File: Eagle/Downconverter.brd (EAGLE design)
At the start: 40 x 40 mm, 26 parts, among them J2 3.5HEADPHONEJACK, J5 U.FL_CONN, J6 U.FL_CONN, U1 5V_REG, U2 MIXER, U3 DUAL_OP_AMP_LMV822, U4 DIGITAL_POTDIGITAL_POT

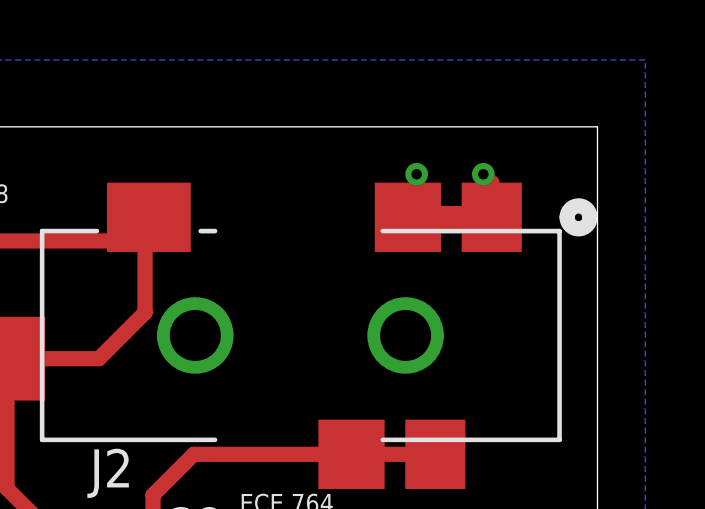
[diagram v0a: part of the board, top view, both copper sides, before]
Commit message: Updated Eagle to 9.4
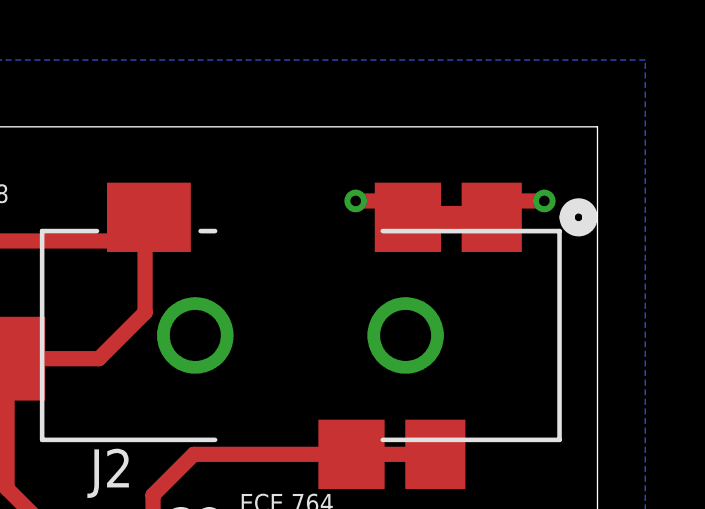
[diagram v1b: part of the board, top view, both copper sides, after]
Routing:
- net GND: track 44.1 -> 45.3 mm
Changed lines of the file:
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@@
 <wire x1="9.74" y1="36.195" x2="11.43" y2="36.195" width="0.762" layer="1"/>
 <via x="11.43" y="36.195" extent="1-16" drill="0.8"/>
-<wire x1="33.6804" y1="36.983" x2="33.9725" y2="37.2751" width="0.508" layer="1"/>
-<wire x1="33.9725" y1="37.2751" x2="33.9725" y2="38.4175" width="0.508" layer="1"/>
-<via x="33.9725" y="38.4175" extent="1-16" drill="0.35"/>
+<wire x1="33.6804" y1="36.983" x2="33.1349" y2="37.5285" width="0.508" layer="1"/>
+<wire x1="33.1349" y1="37.5285" x2="31.9405" y2="37.5285" width="0.508" layer="1"/>
+<via x="31.9405" y="37.5285" extent="1-16" drill="0.35"/>
 <wire x1="36.4744" y1="36.983" x2="36.322" y2="37.1354" width="0.508" layer="1"/>
-<wire x1="36.4744" y1="36.983" x2="36.4744" y2="38.1381" width="0.508" layer="1"/>
-<wire x1="36.4744" y1="38.1381" x2="36.195" y2="38.4175" width="0.508" layer="1"/>
-<via x="36.195" y="38.4175" extent="1-16" drill="0.35"/>
+<wire x1="38.227" y1="37.5285" x2="36.4744" y2="37.5285" width="0.508" layer="1"/>
+<wire x1="36.4744" y1="37.5285" x2="36.4744" y2="36.983" width="0.508" layer="1"/>
+<via x="38.227" y="37.5285" extent="1-16" drill="0.35"/>
 <wire x1="28.2575" y1="11.7613" x2="28.2575" y2="10.16" width="0.4064" layer="1"/>
 <wire x1="28.2575" y1="10.16" x2="28.214875" y2="10.117375" width="0.4064" layer="1"/>

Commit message: update
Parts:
- removed R1: 330, 764Library:R0603
- removed R2: 110, 764Library:R0603
- added C10: 100uF, 764Library:R0603
- added C11: 470pF, 764Library:R0603
- added C9: 10uF, 764Library:R0603
- added R10, R7, R8, R9: 1k, 764Library:R0603
- added U5: TC1185-3.3VCT713, 764Library:SOT-23-5_MC
- C3, C4: value 1uF -> 5.6uF
- C8: value 1uF -> 100uF; device 764Library:R0603 -> 764Library:EXV-9G
- moved J1 92.9 mm to (94.6, 41.3)
- moved J3 90.1 mm to (94.7, 32.6), turned to 270 degrees
- moved C1 89.6 mm to (91.4, 38.7), turned to 180 degrees
- moved J8 77.3 mm to (94.6, 48.9), turned to 270 degrees
- moved J2 74.8 mm to (95.4, 63.0), turned to 270 degrees
- moved U1 74.6 mm to (83.2, 47.6), turned to 90 degrees
- moved J4 72.3 mm to (94.6, 25.1), turned to 270 degrees
- moved C8 63.4 mm to (79.5, 58.9), turned to 90 degrees
- moved J7 57.3 mm to (94.7, 2.79)
- moved U4 55.9 mm to (84.1, 11.4)
- moved C2 3.17 mm to (8.89, 33.0)
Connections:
- removed net N$1: R1.2, R2.1, U1.1
- removed net N$12: C8.1, U3.7, U4.9
- new net AUDIO_OUTPUT: C8.2, J2.3, J2.4, J2.7, J2.8
- new net N$5: C11.1, U5.4
- net 3.3V: now also C10.1, C6.1, R10.1, R7.1, U3.8, U5.5; no longer J4.2
- net 5V: now also C9.1, U5.1, U5.3; no longer C6.1, R2.2, U3.8
- net 9V: now also J4.2
- net GND: now also C10.2, C11.2, C9.2, R8.2, R9.2, U1.1, U5.2; no longer R1.1
- net N$4: now also R7.2, R8.1
- net N$8: now also R10.2, R9.1
- net RDR_OUT: now also C8.1, U3.7, U4.9; no longer C8.2, J2.3, J2.4, J2.7, J2.8
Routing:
- net RDR_OUT: track 38.5 -> 0.04 mm
- net N$12: track 38.1 -> 0.00 mm, vias 2 -> 0
- net AUDIO_OUTPUT: track 0.00 -> 36.6 mm
- net N$13: track 23.7 -> 0.00 mm
- net 9V: track 21.1 -> 40.8 mm
- net GND: track 45.3 -> 25.9 mm, vias 23 -> 14
- net N$4: track 16.5 -> 0.00 mm
- net N$6: track 15.6 -> 0.00 mm
- net 3.3V: track 12.5 -> 0.19 mm
- net 5V: track 51.8 -> 41.7 mm, vias 1 -> 0
- net N$9: track 7.74 -> 0.00 mm
- net N$1: track 7.62 -> 0.00 mm
- net N$7: track 7.18 -> 0.21 mm
- net N$8: track 4.50 -> 0.10 mm
- net SDI: track 10.3 -> 13.2 mm
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- removed copper zone on layer 16, net GND
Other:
- board size 40 x 40 mm -> 100 x 75 mm
- board text added: "+9V"
- board text added: "K.I.S.S. RADAR INC DOWNCONVERTER/PREAMP MIRANDA DODSON REV 0"
- board text removed: "+"
- board text removed: "3.3 V"
- board text removed: "ECE 764 K.I.S.S. Radar DOWNCONVERTER/PREAMP MIRANDA DODSON REV 0"
- board text removed: "TP1"
